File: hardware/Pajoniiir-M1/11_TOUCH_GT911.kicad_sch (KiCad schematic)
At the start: 17 parts

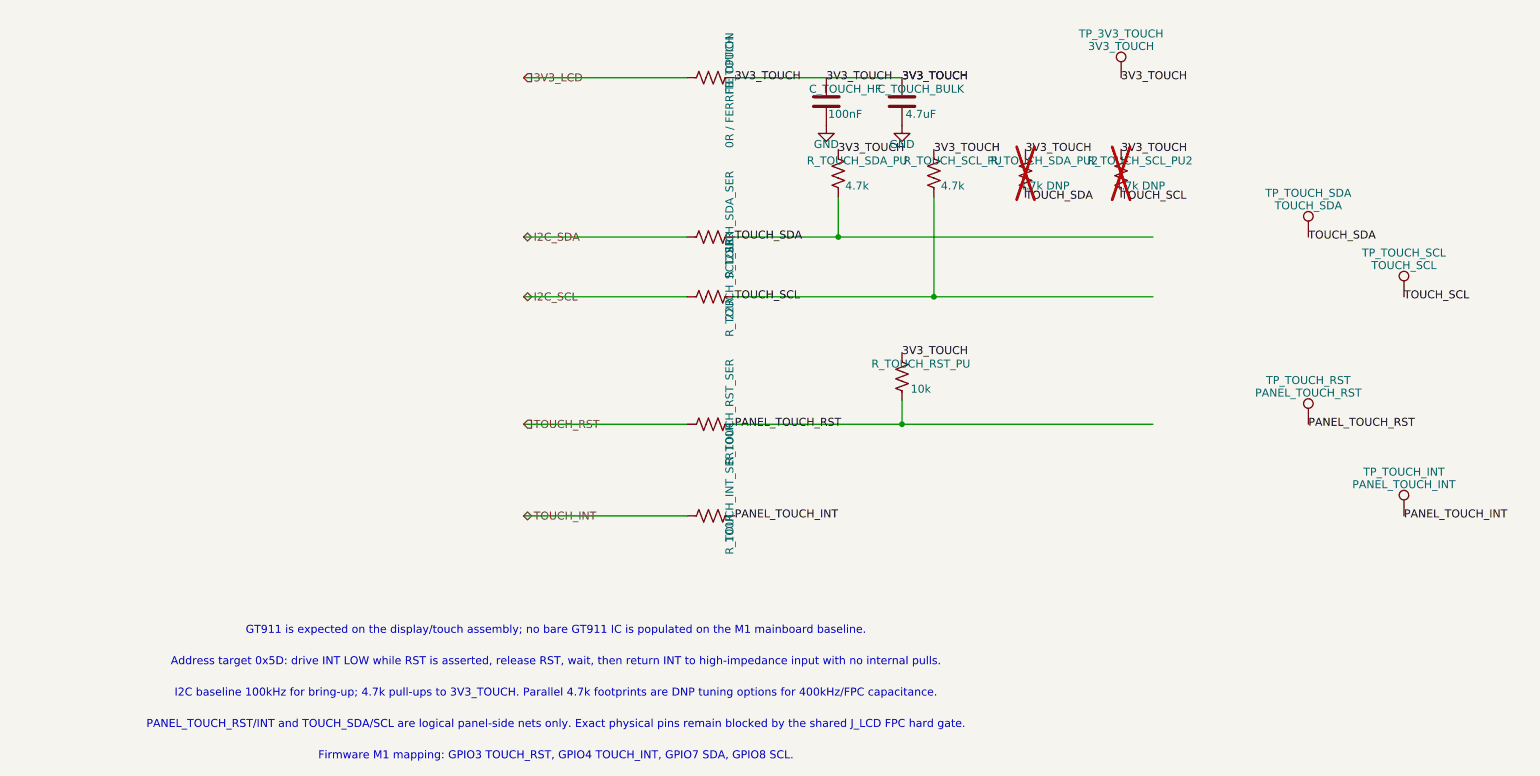
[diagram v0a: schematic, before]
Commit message: hardware: normalize schematic reference designators
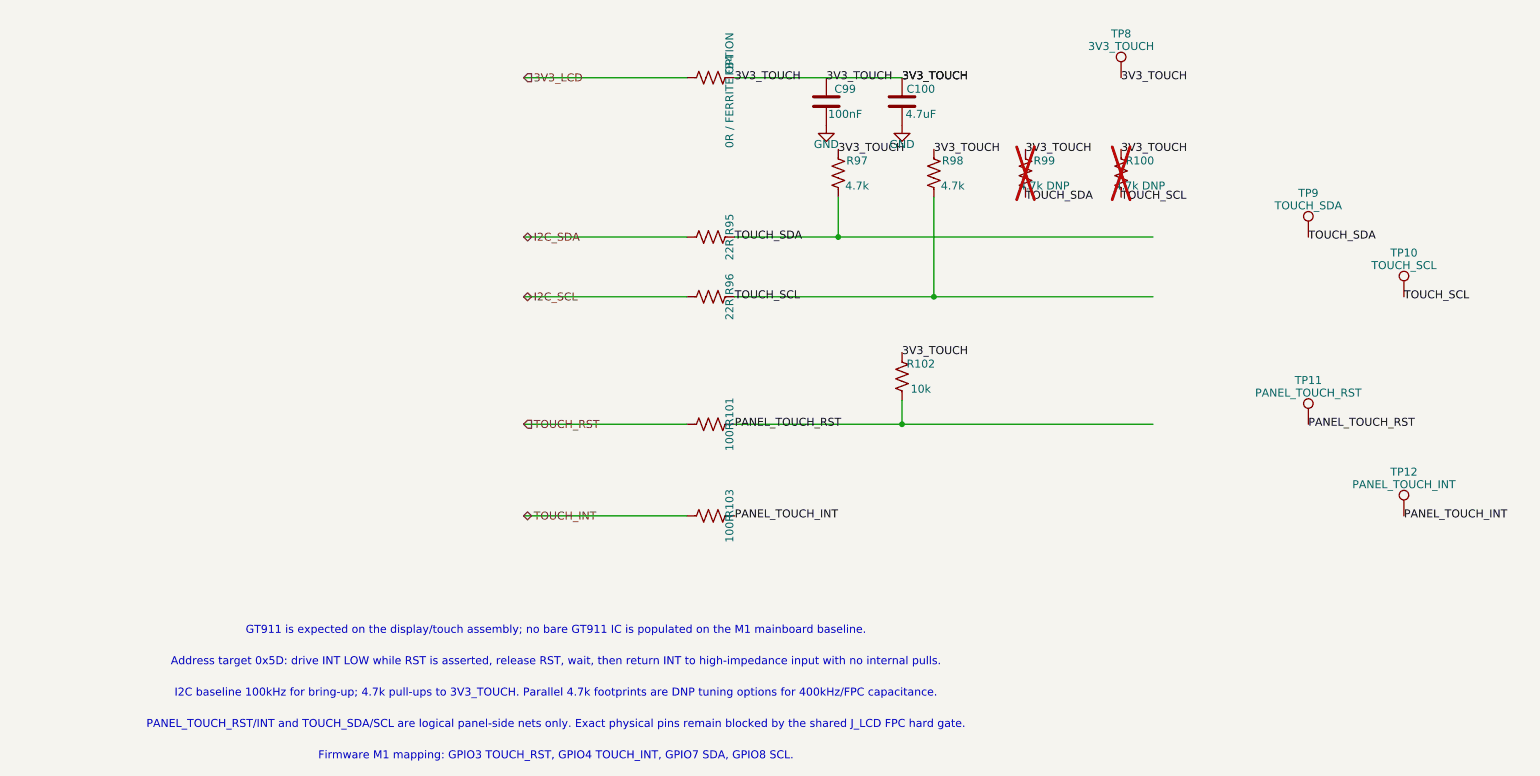
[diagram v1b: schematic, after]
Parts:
- renumbered C_TOUCH_BULK to C100, C_TOUCH_HF to C99, FB_TOUCH to FB4, R_TOUCH_SCL_PU2 to R100, R_TOUCH_RST_SER to R101, R_TOUCH_RST_PU to R102, R_TOUCH_INT_SER to R103, R_TOUCH_SDA_SER to R95, R_TOUCH_SCL_SER to R96, R_TOUCH_SDA_PU to R97, R_TOUCH_SCL_PU to R98, R_TOUCH_SDA_PU2 to R99, TP_TOUCH_SCL to TP10, TP_TOUCH_RST to TP11, TP_TOUCH_INT to TP12, TP_3V3_TOUCH to TP8, TP_TOUCH_SDA to TP9
